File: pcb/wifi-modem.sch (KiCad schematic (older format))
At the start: 55 parts, among them J1 USB_B, J2 Conn_01x03, J3 RS232 DB9, Q1 Q_NPN_BEC, Q2 Q_NPN_BEC, SW1 SW_Push, U1 ESP-12F, U2 74HC245, U3 LM1117-3.3, U4 FT232RL, U5 MAX232

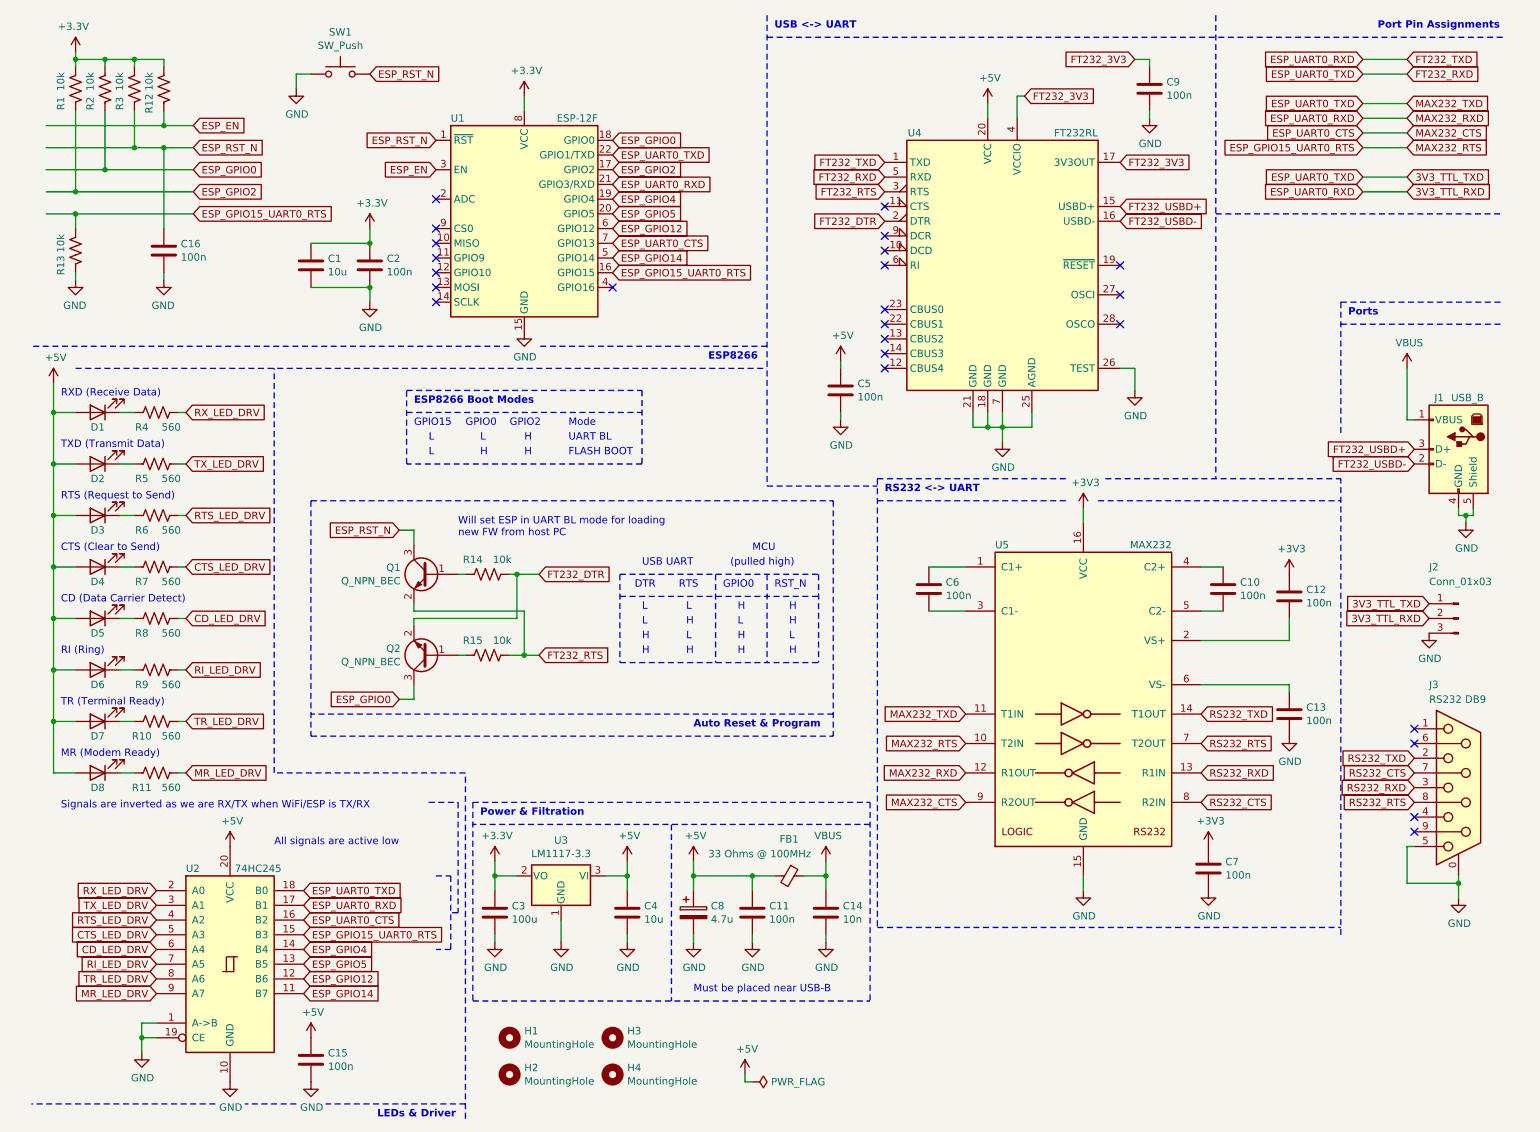
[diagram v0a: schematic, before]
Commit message: Added transceiver control
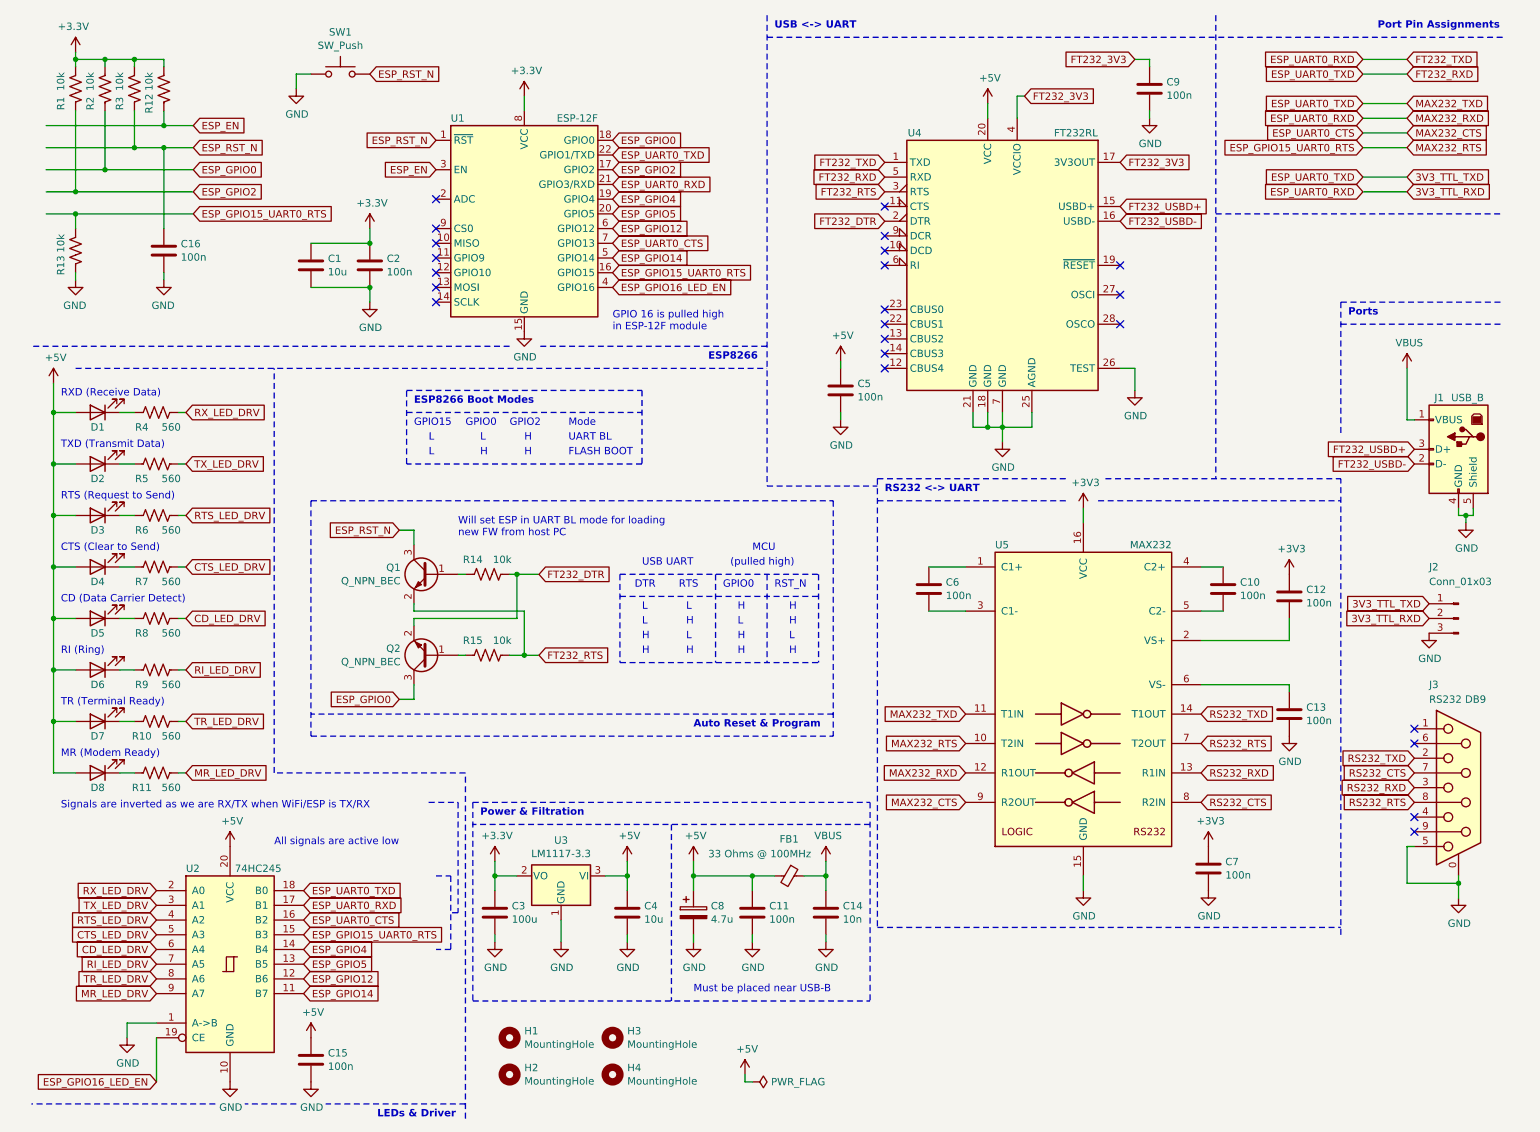
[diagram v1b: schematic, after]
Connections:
- net labels added: ESP_GPIO16_LED_EN
- wire segments 156 -> 155
- no-connect marks 24 -> 23
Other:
- note added: "GPIO 16 is pulled high\nin ESP-12F module"
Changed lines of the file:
@@
-	1    0    0    -1
-$EndComp
-Wire Wire Line
-	1250 7450 1250 7550
-Connection ~ 1250 7450
-Wire Wire Line
-	1350 7450 1250 7450
-Wire Wire Line
-	1250 7350 1250 7450
-Wire Wire Line
-	1350 7350 1250 7350
-$Comp
-L power:GND #PWR03
-U 1 1 5F11E723
-P 1250 7550
-F 0 "#PWR03" H 1250 7300 50  0001 C CNN
-F 1 "GND" H 1255 7377 50  0000 C CNN
-F 2 "" H 1250 7550 50  0001 C CNN
-F 3 "" H 1250 7550 50  0001 C CNN
-	1    1250 7550
 	1    0    0    -1
 $EndComp
@@
 NoConn ~ 6300 2600
 NoConn ~ 6300 2500
-NoConn ~ 4450 2350
 NoConn ~ 3250 2450
 NoConn ~ 3250 2350
@@
 Wire Wire Line
 	2800 1950 2800 2050
+Text GLabel 4450 2350 2    50   Input ~ 0
+ESP_GPIO16_LED_EN
+Text Notes 4450 2650 0    50   ~ 0
+GPIO 16 is pulled high\nin ESP-12F module
+Text GLabel 1350 7750 0    50   Input ~ 0
+ESP_GPIO16_LED_EN
+Wire Wire Line
+	1350 7450 1350 7750
+Wire Wire Line
+	1350 7350 1150 7350
+Wire Wire Line
+	1150 7350 1150 7450
+$Comp
+L power:GND #PWR0102
+U 1 1 5F711E40
+P 1150 7450
+F 0 "#PWR0102" H 1150 7200 50  0001 C CNN
+F 1 "GND" H 1155 7277 50  0000 C CNN
+F 2 "" H 1150 7450 50  0001 C CNN
+F 3 "" H 1150 7450 50  0001 C CNN
+	1    1150 7450
+	1    0    0    -1
+$EndComp
 $EndSCHEMATC

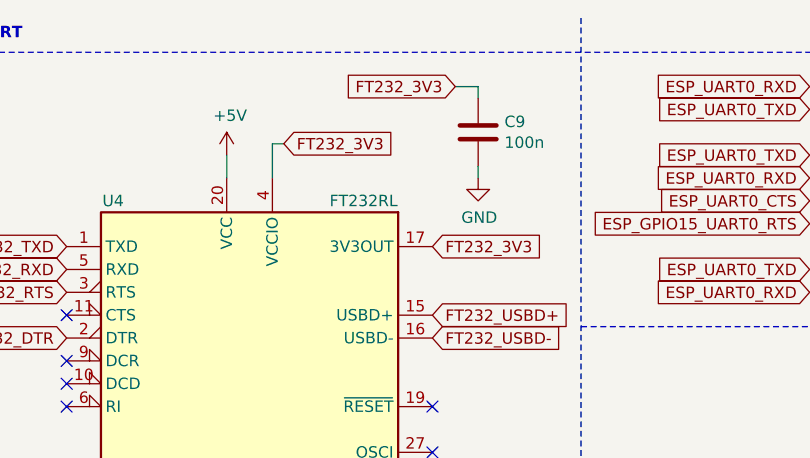
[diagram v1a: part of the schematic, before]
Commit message: Changing VCCIO supply to external 3V3 LDO
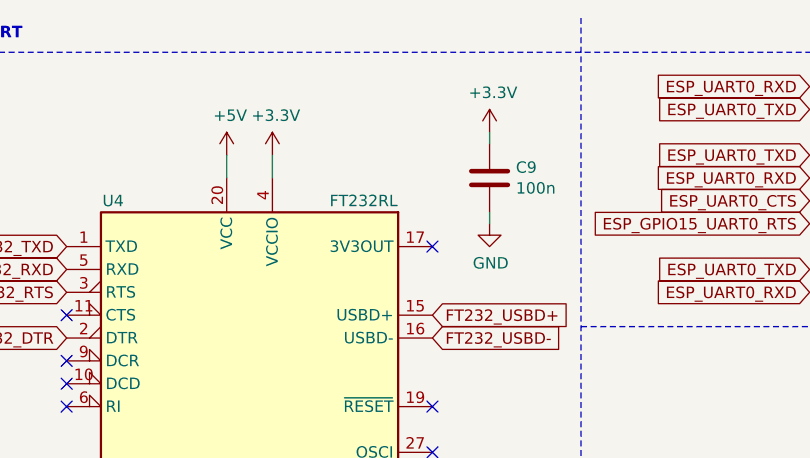
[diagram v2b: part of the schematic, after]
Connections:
- net labels removed: FT232_3V3
- wire segments 155 -> 153
- no-connect marks 23 -> 24
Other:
- moved on the sheet: C9
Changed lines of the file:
@@
 Title "WiFi Modem"
 Date "2020-08-31"
-Rev "2.0"
+Rev "2.1"
 Comp "Michel Kakulphimp - VA7XMK"
 Comment1 ""
@@
 L Device:C C9
 U 1 1 5FB63B3E
-P 8100 1000
-F 0 "C9" H 8215 1046 50  0000 L CNN
-F 1 "100n" H 8215 955 50  0000 L CNN
-F 2 "Capacitor_SMD:C_0805_2012Metric_Pad1.15x1.40mm_HandSolder" H 8138 850 50  0001 C CNN
-F 3 "~" H 8100 1000 50  0001 C CNN
-	1    8100 1000
+P 8150 1200
+F 0 "C9" H 8265 1246 50  0000 L CNN
+F 1 "100n" H 8265 1155 50  0000 L CNN
+F 2 "Capacitor_SMD:C_0805_2012Metric_Pad1.15x1.40mm_HandSolder" H 8188 1050 50  0001 C CNN
+F 3 "~" H 8150 1200 50  0001 C CNN
+	1    8150 1200
 	1    0    0    -1
 $EndComp
 Wire Wire Line
 	8000 2900 8000 3050
-Text GLabel 7250 1050 2    50   Input ~ 0
-FT232_3V3
-Text GLabel 7900 1500 2    50   Input ~ 0
-FT232_3V3
-Text GLabel 8000 800  0    50   Input ~ 0
-FT232_3V3
-Wire Wire Line
-	8000 800  8100 800
-Wire Wire Line
-	8100 800  8100 850
+Wire Wire Line
+	8150 1000 8150 1050
 $Comp
 L power:GND #PWR029
 U 1 1 5FB9B45B
-P 8100 1200
-F 0 "#PWR029" H 8100 950 50  0001 C CNN
-F 1 "GND" H 8105 1027 50  0000 C CNN
-F 2 "" H 8100 1200 50  0001 C CNN
-F 3 "" H 8100 1200 50  0001 C CNN
-	1    8100 1200
-	1    0    0    -1
-$EndComp
-Wire Wire Line
-	8100 1150 8100 1200
+P 8150 1400
+F 0 "#PWR029" H 8150 1150 50  0001 C CNN
+F 1 "GND" H 8155 1227 50  0000 C CNN
+F 2 "" H 8150 1400 50  0001 C CNN
+F 3 "" H 8150 1400 50  0001 C CNN
+	1    8150 1400
+	1    0    0    -1
+$EndComp
+Wire Wire Line
+	8150 1350 8150 1400
 NoConn ~ 7900 2600
 NoConn ~ 7900 2400
@@
 Text GLabel 4450 1550 2    50   Input ~ 0
 ESP_GPIO2
-Wire Wire Line
-	7200 1050 7250 1050
-Wire Wire Line
-	7200 1050 7200 1200
 $Comp
 L power:PWR_FLAG #FLG0101
@@
 	1    0    0    -1
 $EndComp
+NoConn ~ 7900 1500
+$Comp
+L power:+3.3V #PWR0103
+U 1 1 5F9C7B54
+P 7200 1100
+F 0 "#PWR0103" H 7200 950 50  0001 C CNN
+F 1 "+3.3V" H 7215 1273 50  0000 C CNN
+F 2 "" H 7200 1100 50  0001 C CNN
+F 3 "" H 7200 1100 50  0001 C CNN
+	1    7200 1100
+	1    0    0    -1
+$EndComp
+Wire Wire Line
+	7200 1100 7200 1200
+$Comp
+L power:+3.3V #PWR?
+U 1 1 5F9D6971
+P 8150 1000
+F 0 "#PWR?" H 8150 850 50  0001 C CNN
+F 1 "+3.3V" H 8165 1173 50  0000 C CNN
+F 2 "" H 8150 1000 50  0001 C CNN
+F 3 "" H 8150 1000 50  0001 C CNN
+	1    8150 1000
+	1    0    0    -1
+$EndComp

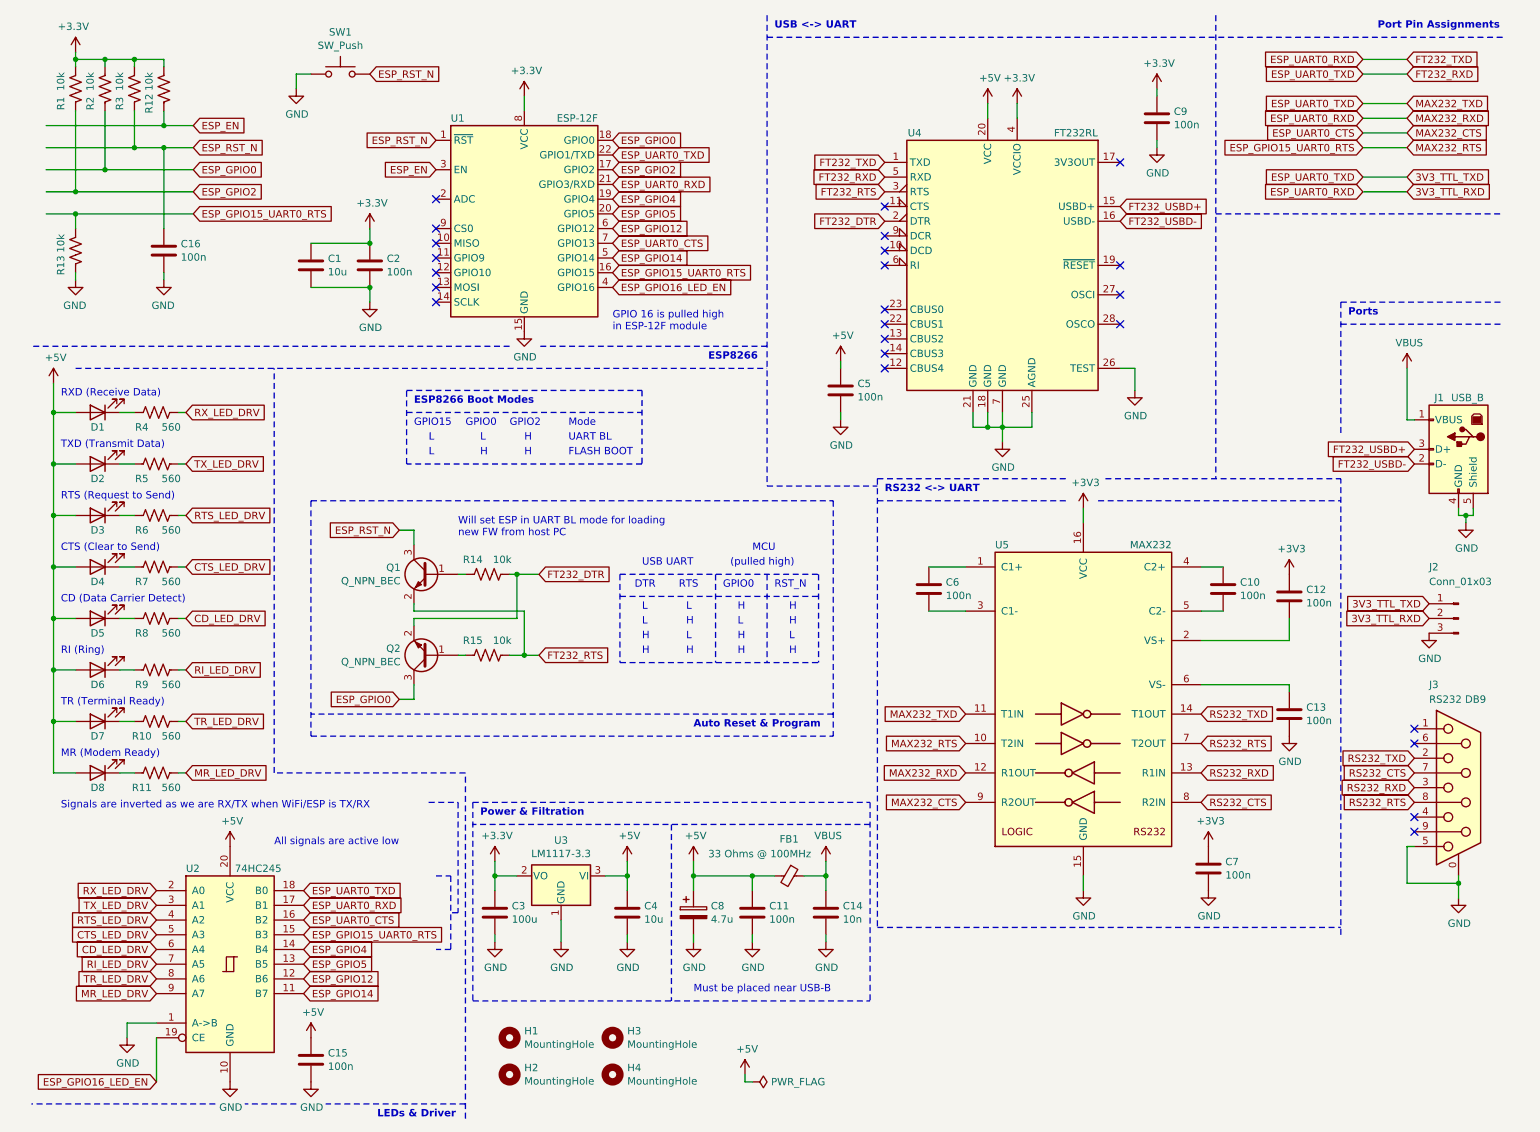
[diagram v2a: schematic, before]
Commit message: Rev 2.1 updates
* Added 3-input AND to handle 3x serial inputs
* Added manual UART BL mode jumper
* Changed footprint of 2 transistors
* Updated refdes of caps
* Using 3V3 LDO for FT232RL IO
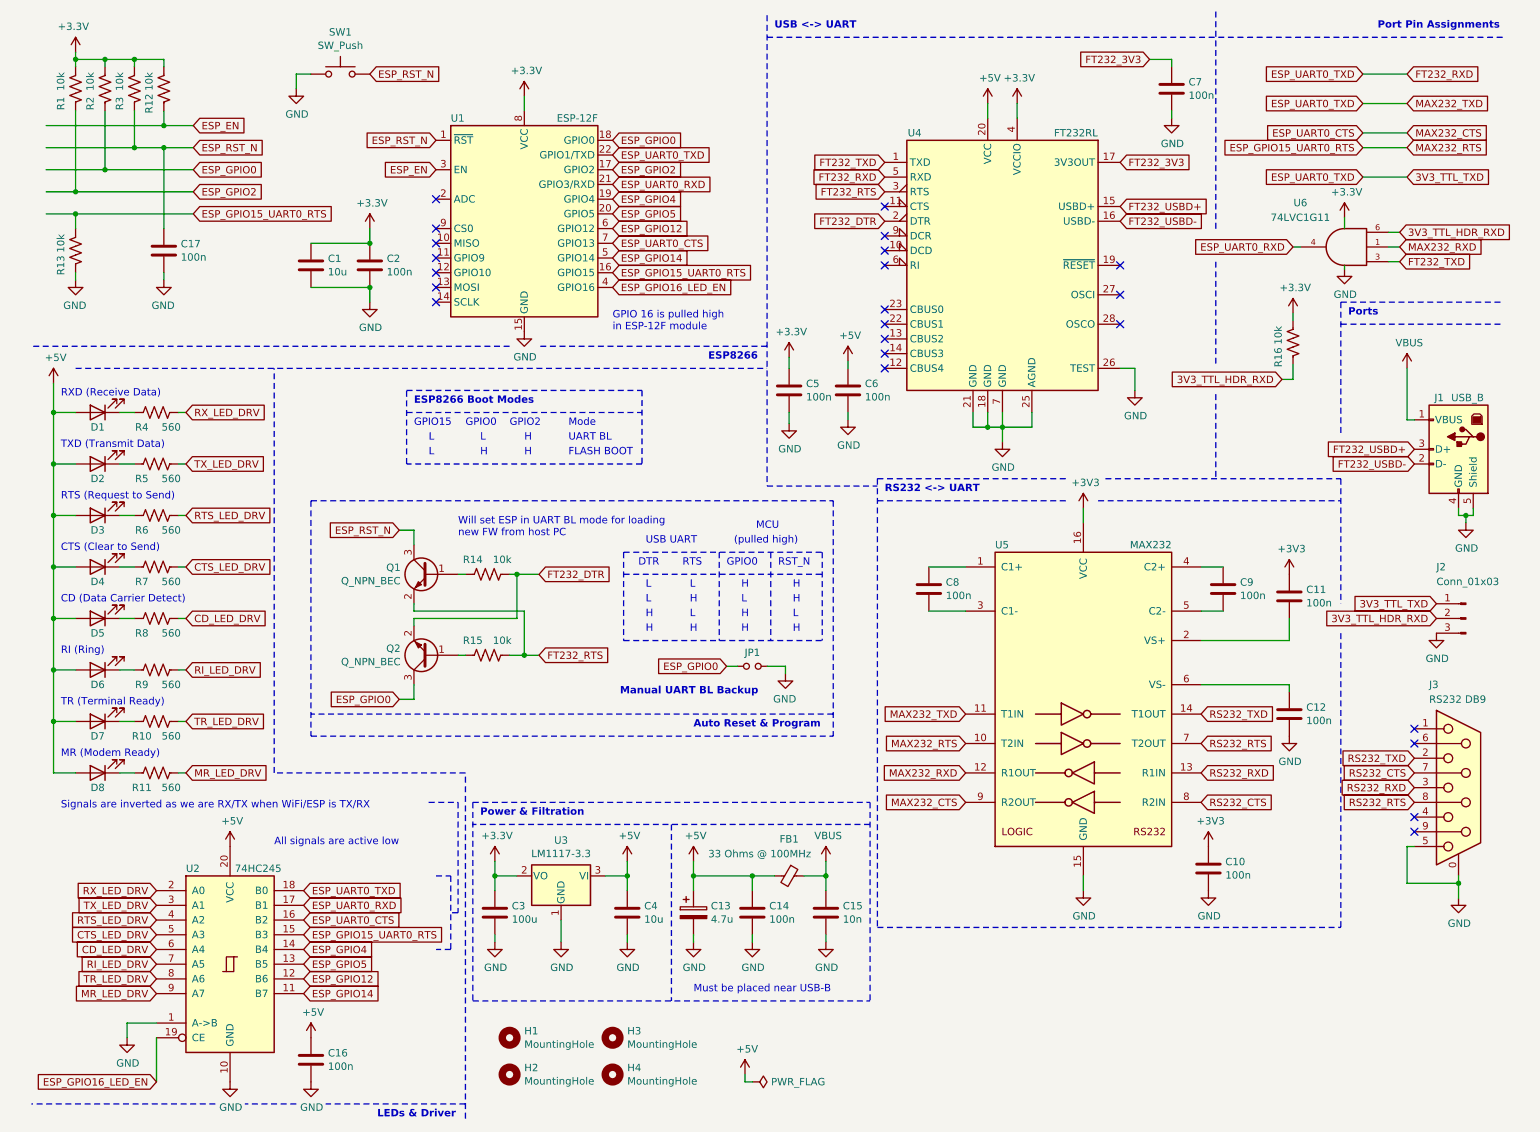
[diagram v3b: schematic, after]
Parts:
- added C5: 100n, Capacitor_SMD:C_0805_2012Metric_Pad1.15x1.40mm_HandSolder, symbol Device:C
- added JP1: Jumper_NO_Small, Connector_PinHeader_2.54mm:PinHeader_1x02_P2.54mm_Vertical, symbol Device:Jumper_NO_Small
- added R16: 10k, Resistor_SMD:R_0805_2012Metric_Pad1.15x1.40mm_HandSolder, symbol Device:R_US
- added U6: 74LVC1G11, Package_TO_SOT_SMD:SOT-23-6_Handsoldering, symbol 74xGxx:74LVC1G11
- Q1, Q2: footprint Package_TO_SOT_SMD:SOT-23 -> Package_TO_SOT_SMD:SOT-23_Handsoldering
- renumbered C7 to C10, C12 to C11, C13 to C12, C8 to C13, C11 to C14, C14 to C15, C15 to C16, C16 to C17, C5 to C6, C9 to C7, C6 to C8, C10 to C9
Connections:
- net labels added: 3V3_TTL_HDR_RXD, FT232_3V3
- net labels removed: 3V3_TTL_RXD
- wire segments 153 -> 165
- no-connect marks 24 -> 23
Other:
- note added: "Manual UART BL Backup"
- moved on the sheet: C6, C7, J2
